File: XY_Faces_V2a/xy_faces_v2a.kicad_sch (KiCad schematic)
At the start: 26 parts, among them CN1 DF13A-5P-1.25H(21), CN2 DF13C-5P-1.25V(21), J2 Conn_01x01, J3 Conn_01x01, J4 Conn_01x01, J5 Conn_01x01, U1 VEML7700, U2 MCP9808_DFN, U3 DRV2605LDGS

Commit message: minor changes
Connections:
- no-connect marks 6 -> 10
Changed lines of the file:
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@@
+	)
+	(no_connect
+		(at 121.92 162.56)
+	)
+	(no_connect
+		(at 121.92 151.13)
+	)
+	(no_connect
+		(at 121.92 182.88)
+	)
+	(no_connect
+		(at 121.92 130.81)
 	)
 	(no_connect

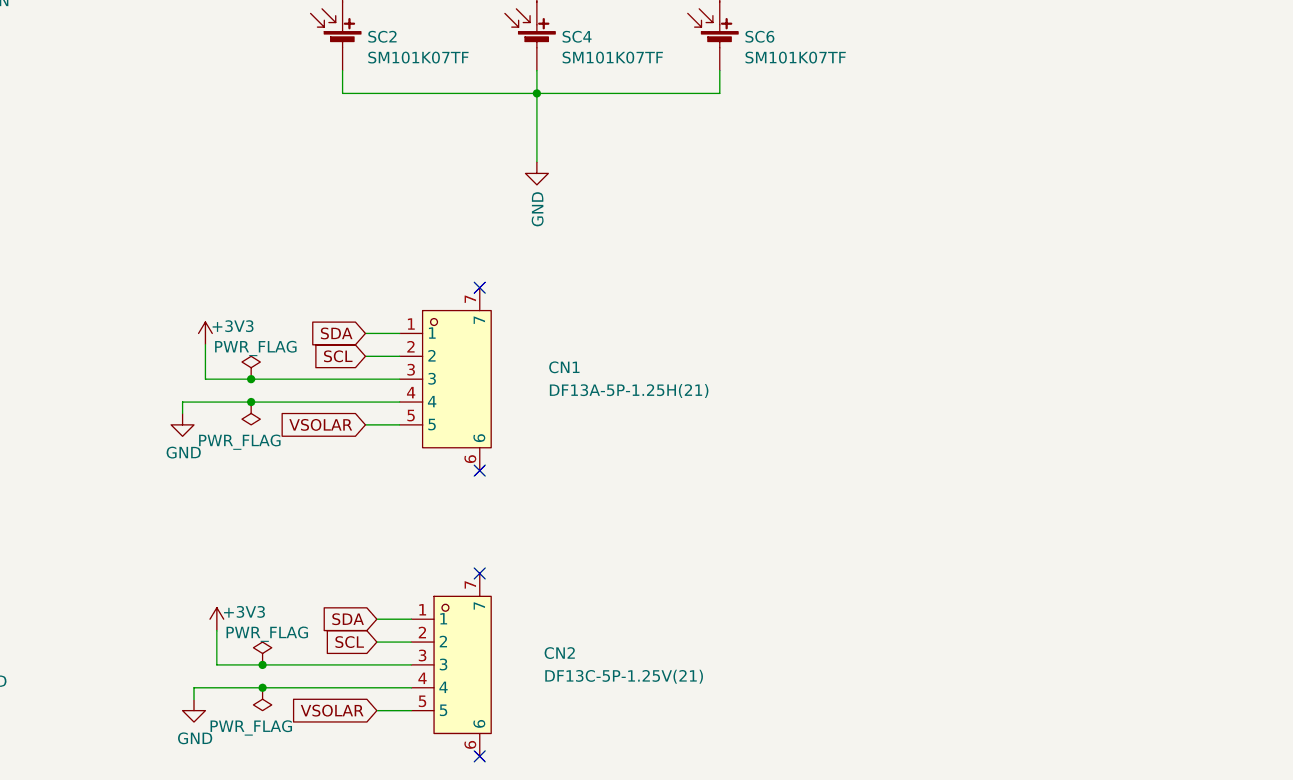
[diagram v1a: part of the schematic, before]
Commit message: Added TCA Buffer
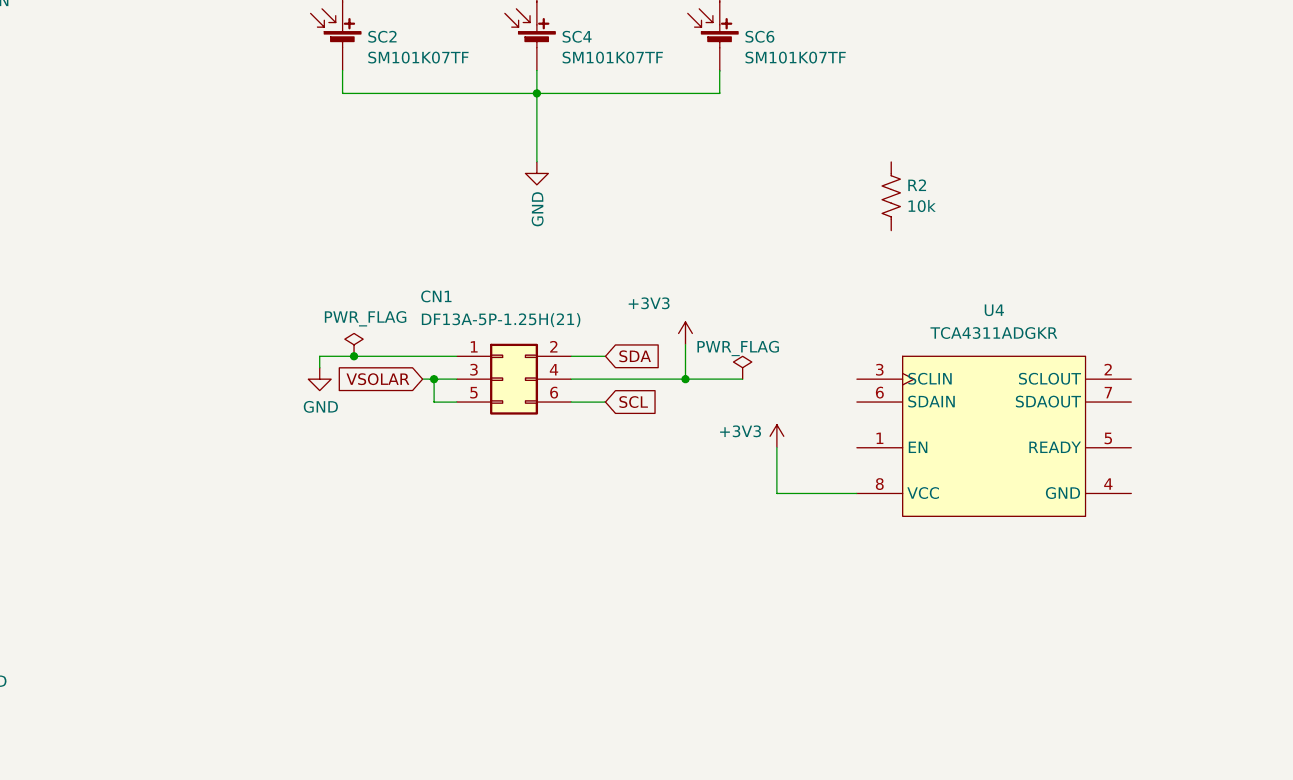
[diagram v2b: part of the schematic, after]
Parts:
- removed CN2: DF13C-5P-1.25V(21), Connector_Hirose:Hirose_DF11-6DP-2DSA_2x03_P2.00mm_Vertical, symbol easyeda2kicad:DF13C-5P-1.25V(21)
- added R2: 10k, Resistor_SMD:R_0603_1608Metric, symbol Device:R_US
- added U4: TCA4311ADGKR, easyeda2kicad:MSOP-8_L3.0-W3.0-P0.65-LS5.0-BL, symbol easyeda2kicad:TCA4311ADGKR
- CN1: symbol easyeda2kicad:DF13A-5P-1.25H(21) -> Connector_Generic:Conn_02x03_Odd_Even
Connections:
- net +3V3: now also CN1.4 (Pin_4), U4.8 (VCC); no longer CN1.3
- net GND: now also CN1.1 (Pin_1); no longer CN1.4
- net SCL: now also CN1.6 (Pin_6); no longer CN1.2
- net SDA: now also CN1.2 (Pin_2); no longer CN1.1
- net VSOLAR: now also CN1.3 (Pin_3)
- no-connect marks 10 -> 6

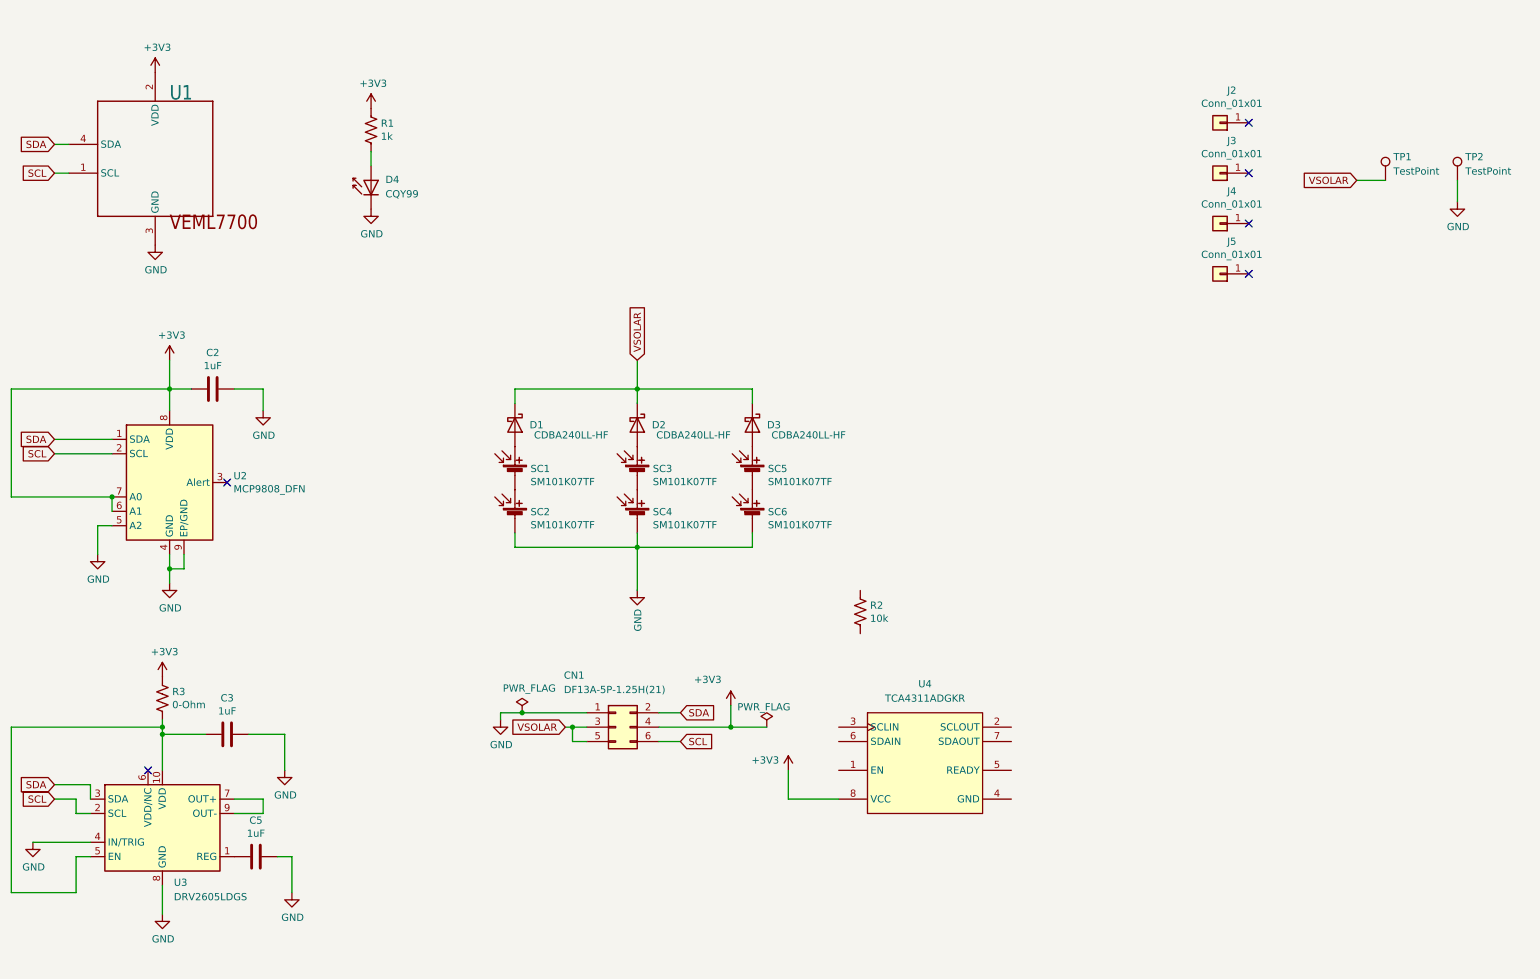
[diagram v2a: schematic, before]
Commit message: Rewired Face
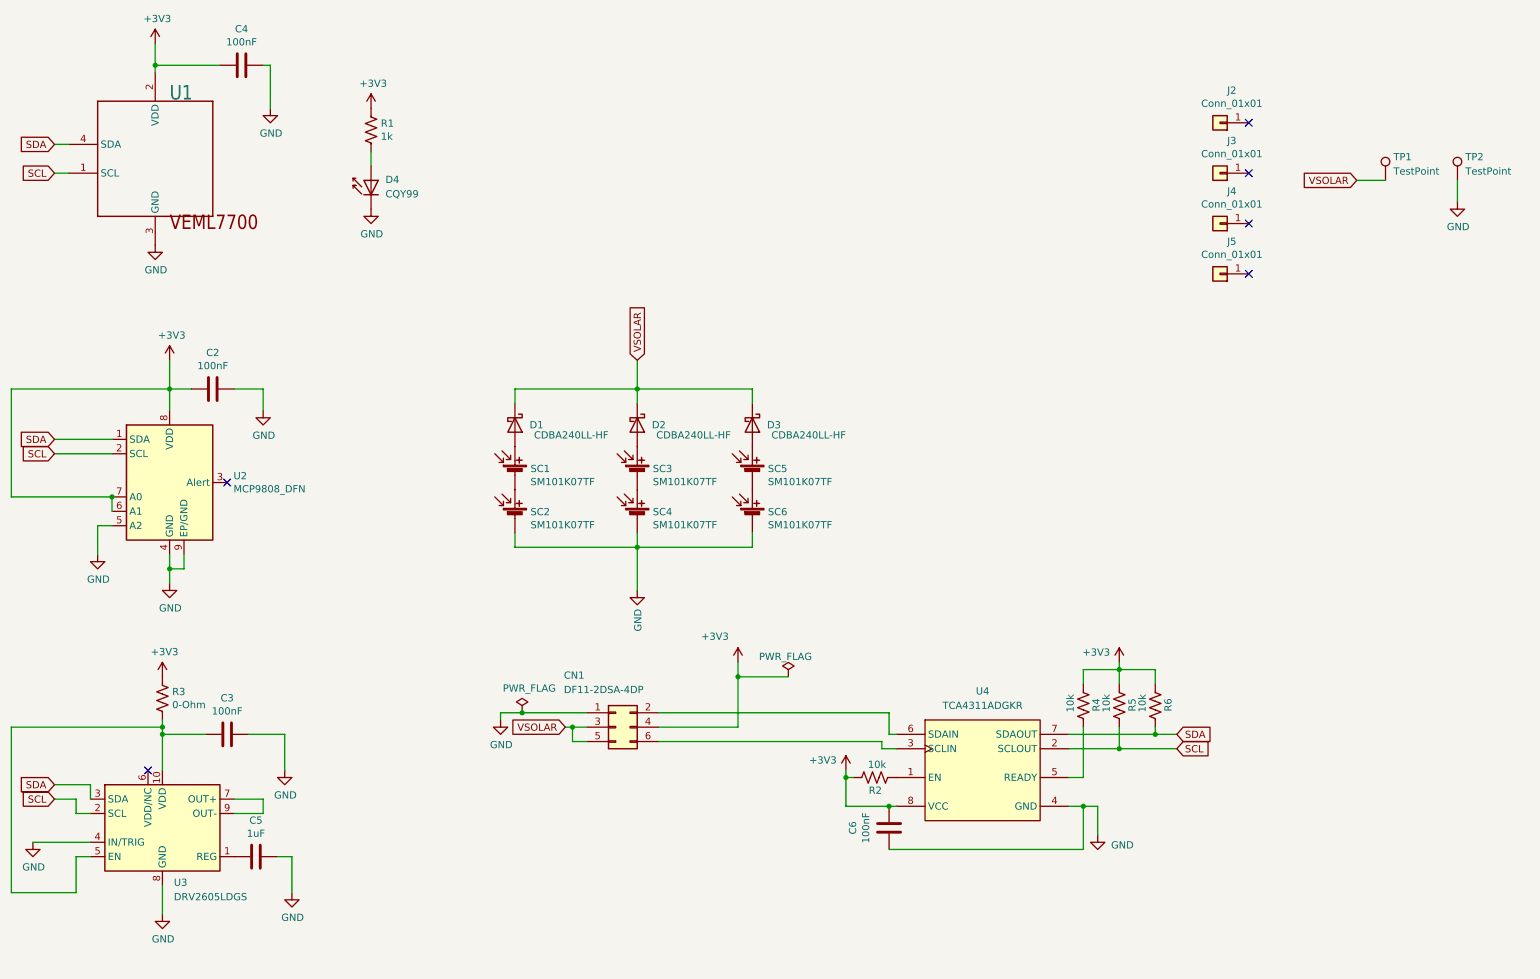
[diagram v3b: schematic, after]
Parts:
- added C4, C6: 100nF, Capacitor_SMD:C_0805_2012Metric, symbol Device:C
- added R4, R5, R6: 10k, Resistor_SMD:R_0603_1608Metric, symbol Device:R_US
- C2, C3: value 1uF -> 100nF
- CN1: value DF13A-5P-1.25H(21) -> DF11-2DSA-4DP
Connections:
- net +3V3: now also R2.1, C4.1, C6.2, R4.2, R5.2, R6.2
- net GND: now also U4.4 (GND), C4.2, C6.1
- net SCL: now also U4.2 (SCLOUT), R5.1; no longer CN1.6 (Pin_6)
- net SDA: now also U4.7 (SDAOUT), R6.1; no longer CN1.2 (Pin_2)
- net at R2.2: now also U4.1 (EN)
- net at U4.3 (SCLIN): now also CN1.6 (Pin_6)
- net at U4.5 (READY): now also R4.1
- net at U4.6 (SDAIN): now also CN1.2 (Pin_2)
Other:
- moved on the sheet: R2, U4
